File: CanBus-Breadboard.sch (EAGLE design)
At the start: 3 parts

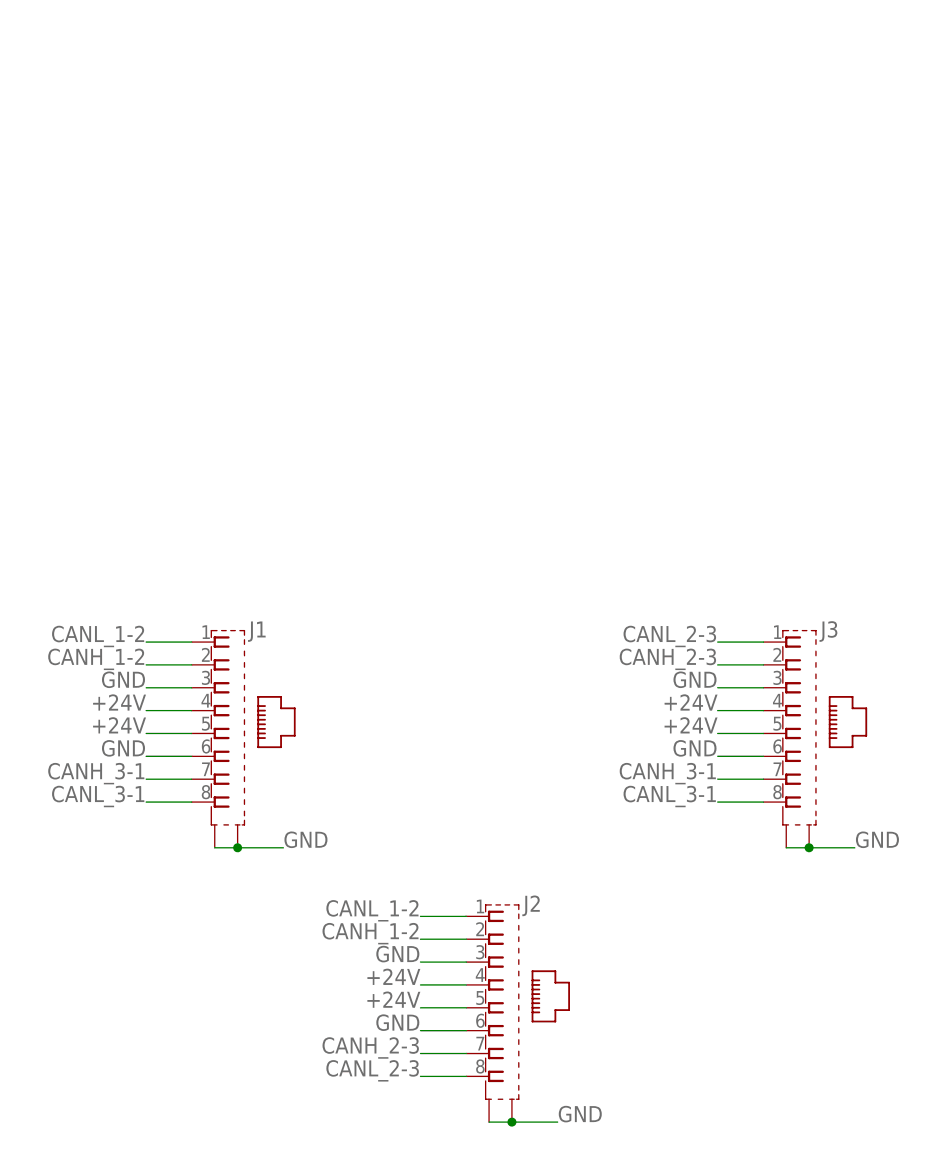
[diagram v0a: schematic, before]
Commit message: CAN-Bus Beadboard-Adapter, Layouts angepasst
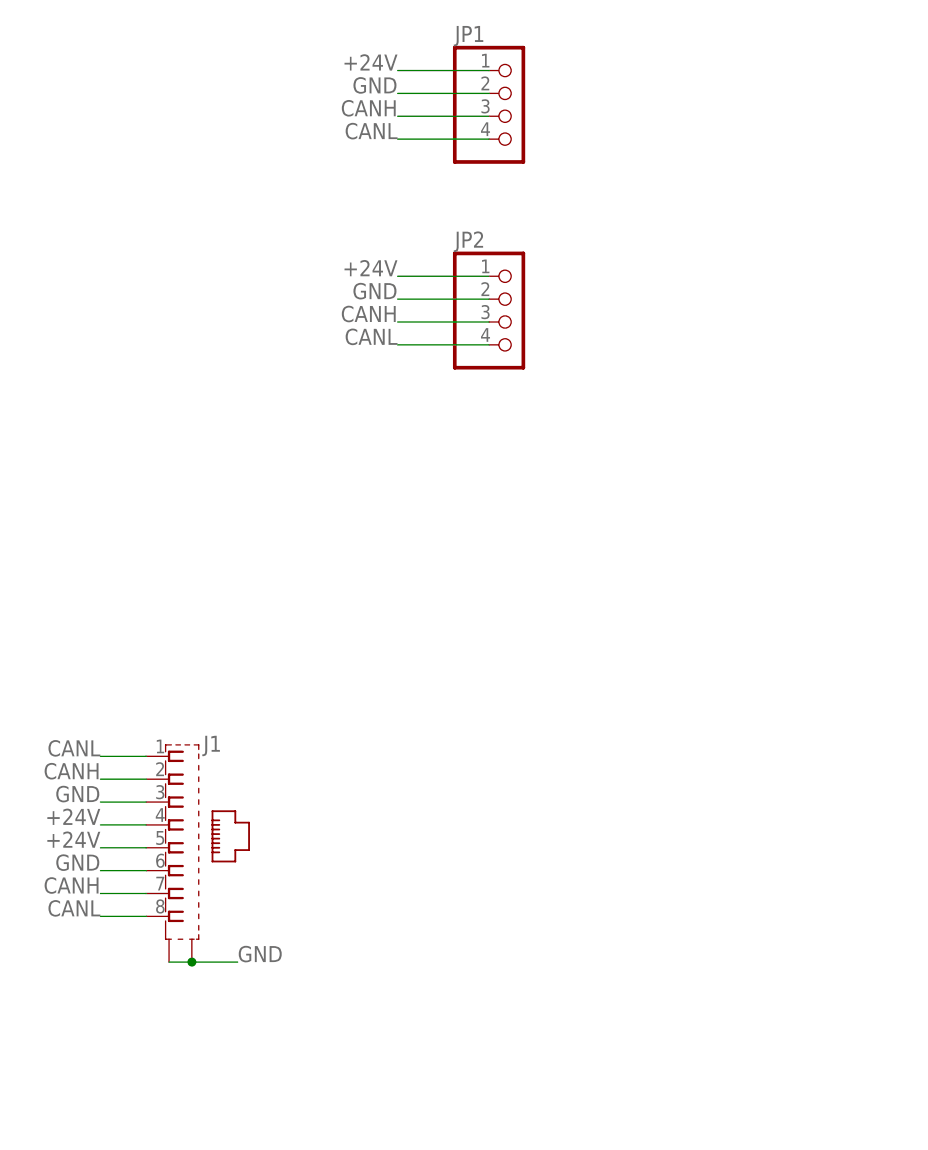
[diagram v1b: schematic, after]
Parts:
- removed J2, J3: (no value), mebp_8-8g:555141-1
- added JP1, JP2: (no value), pinhead:PINHD-1X4
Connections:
- removed net CANH_1-2: J1.2, J2.2
- removed net CANH_2-3: J2.7, J3.2
- removed net CANH_3-1: J1.7, J3.7
- removed net CANL_1-2: J1.1, J2.1
- removed net CANL_2-3: J2.8, J3.1
- removed net CANL_3-1: J1.8, J3.8
- new net CANH: J1.2, J1.7, JP1.3, JP2.3
- new net CANL: J1.1, J1.8, JP1.4, JP2.4
- net +24V: now also JP1.1, JP2.1; no longer J2.4, J2.5, J3.4, J3.5
- net GND: now also JP1.2, JP2.2; no longer J2.3, J2.6, J2.S1, J2.S2, J3.3, J3.6, J3.S1, J3.S2
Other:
- moved on the sheet: J1
